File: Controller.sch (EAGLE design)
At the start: 40 parts, among them SW1 MULTICOLOR_BUTTON, SW2 MULTICOLOR_BUTTON, SW3 MULTICOLOR_BUTTON, SW4 MULTICOLOR_BUTTON, SW5 MULTICOLOR_BUTTON, SW6 MULTICOLOR_BUTTON, SW7 MULTICOLOR_BUTTON, SW8 MULTICOLOR_BUTTON

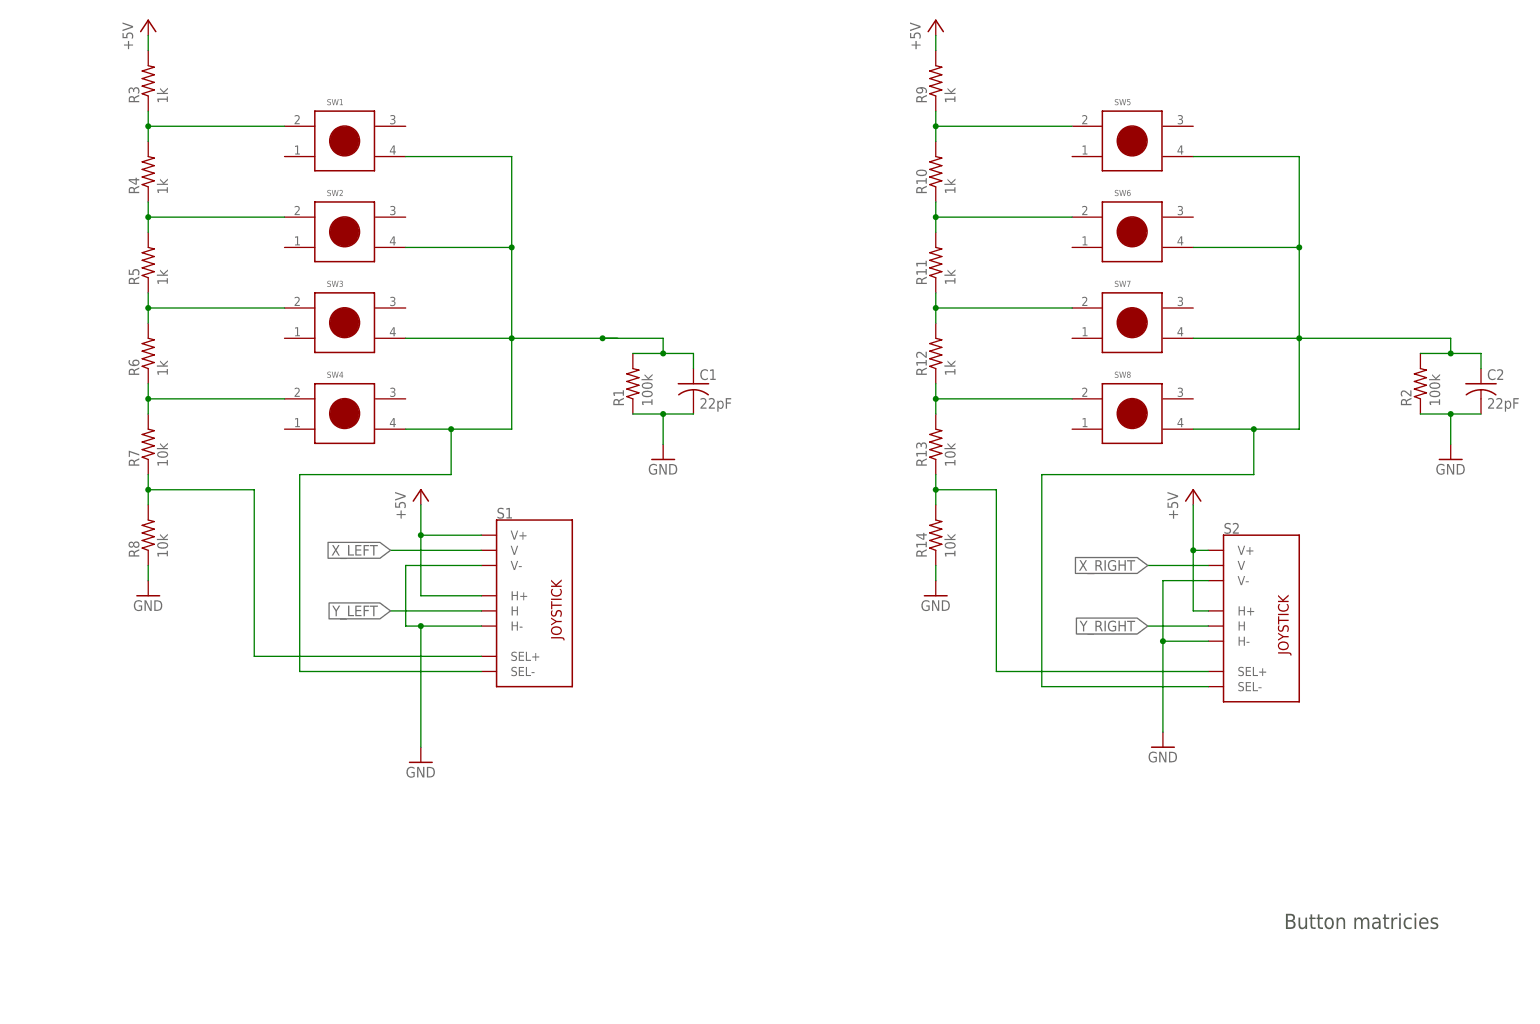
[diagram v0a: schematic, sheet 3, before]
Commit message: Redid debounce filter and added unity gain buffer. Added Xbee and logic level shifter for RX and TX
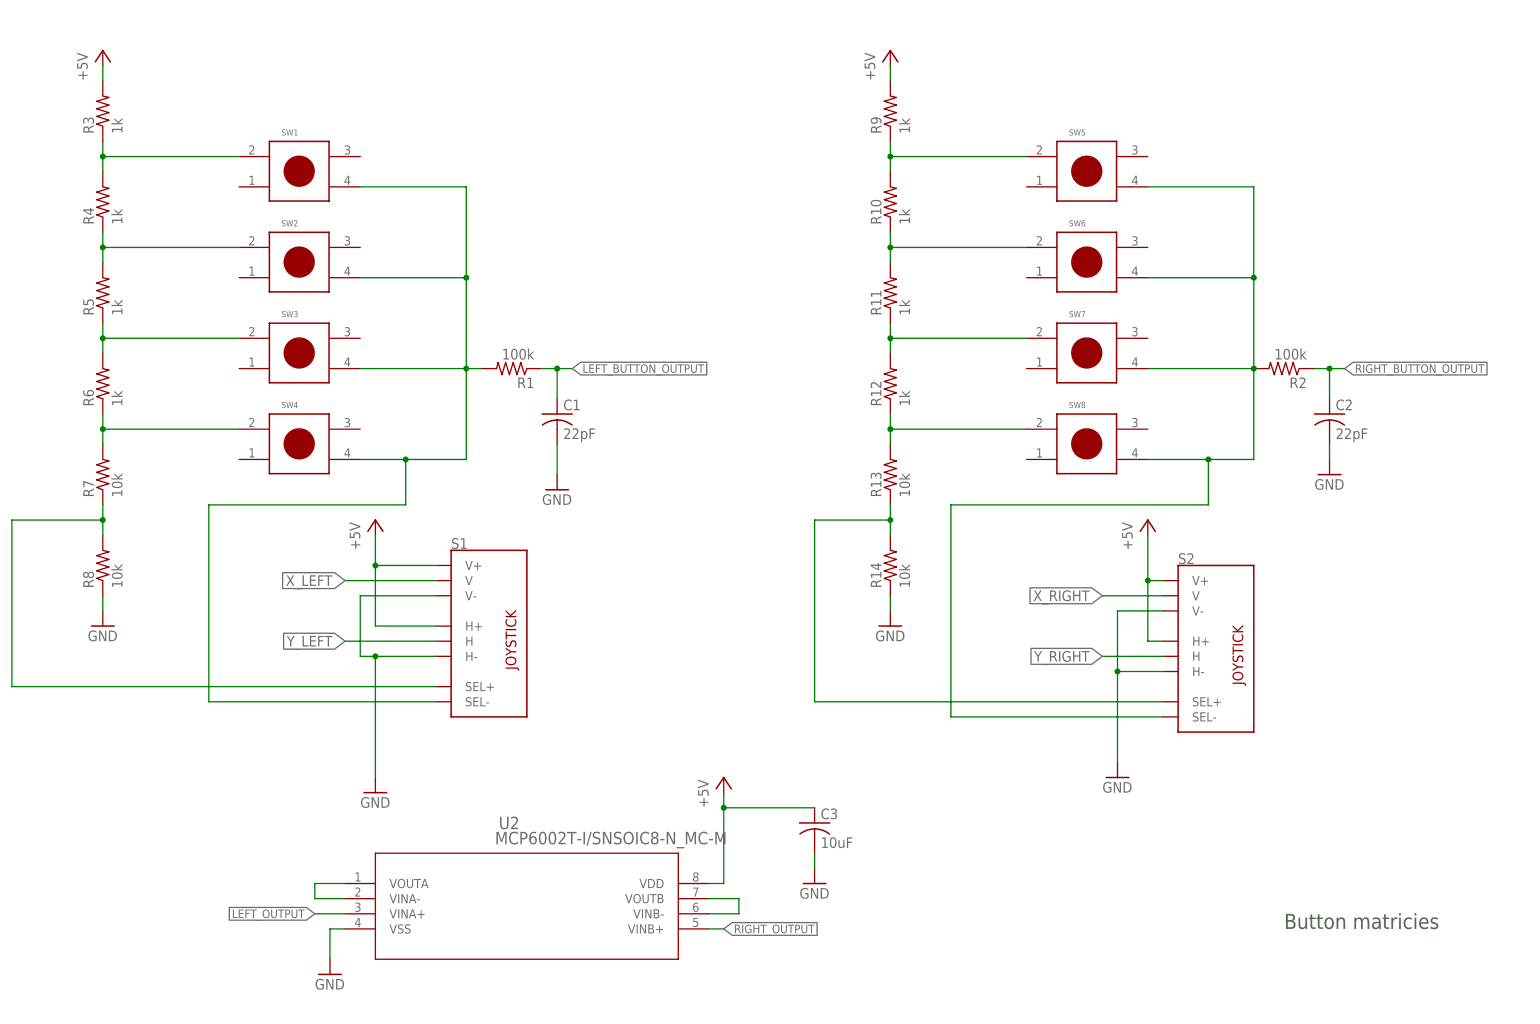
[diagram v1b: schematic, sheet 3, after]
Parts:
- removed U$1: NANO_SKELETON_FOR_PRATIK, Micah's Shit For Pratik:NANO_SKELETON_FOR_PRATIK
- added C3: 10uF, rcl:C-USC1206
- added U1: ATMEGA328-PU, Controller:ATMEGA328-PU
- added U2: MCP6002T-I/SNSOIC8-N_MC-M, Controller:MCP6002T-I/SNSOIC8-N_MC-M
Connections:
- removed net BUT_OUT_L: U$1.1/TX
- removed net BUT_OUT_R: U$1.0/RX
- removed net N$1: C1.1, R1.2, S1.SEL-, SW1.P$4, SW2.P$4, SW3.P$4, SW4.P$4
- new net LEFT_BUTTON_OUTPUT: C1.1, R1.1
- new net LEFT_OUTPUT: R1.2, S1.SEL-, SW1.P$4, SW2.P$4, SW3.P$4, SW4.P$4, U1.PB1/OC1A/PCINT1, U1.PC0/ADC0/PCINT8, U2.VINA+
- new net N$13: U2.VINB-, U2.VOUTB
- new net RIGHT_BUTTON_OUTPUT: C2.1, R2.1
- new net RIGHT_OUTPUT: R2.2, S2.SEL-, SW5.P$4, SW6.P$4, SW7.P$4, SW8.P$4, U1.PC1/ADC1/PCINT9, U1.PCINT23/AIN1/PD7, U2.VINB+
- net +5V: now also C3.1, U1.AREF, U1.VCC, U2.VDD
- net 3.3: no longer U$1.3.3V
- net 5V: no longer U$1.+5V
- net BUT_OUT_BUMP: no longer U$1.7
- net GND: now also C3.2, U1.GND, U1.GND_2, U2.VSS; no longer R1.1, R2.1, U$1.GND, U$1.GND2.0
- net N$2: now also U2.VINA-, U2.VOUTA; no longer C2.1, R2.2, S2.SEL-, SW5.P$4, SW6.P$4, SW7.P$4, SW8.P$4
- net XBEE_DIN: no longer U$1.2/SDA
- net XBEE_DOUT: no longer U$1.3(PWM)/SCL
- net X_LEFT: now also U1.PC2/ADC2/PCINT10
- net X_RIGHT: now also U1.PC4/ADC4/SDA/PCINT12
- net Y_LEFT: now also U1.PC3/ADC3/PCINT11
- net Y_RIGHT: now also U1.PC5/ADC5/SCL/PCINT13
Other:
- moved on the sheet: C1, C2, R1, R10, R11, R12, R13, R14, R2, R3, R4, R5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

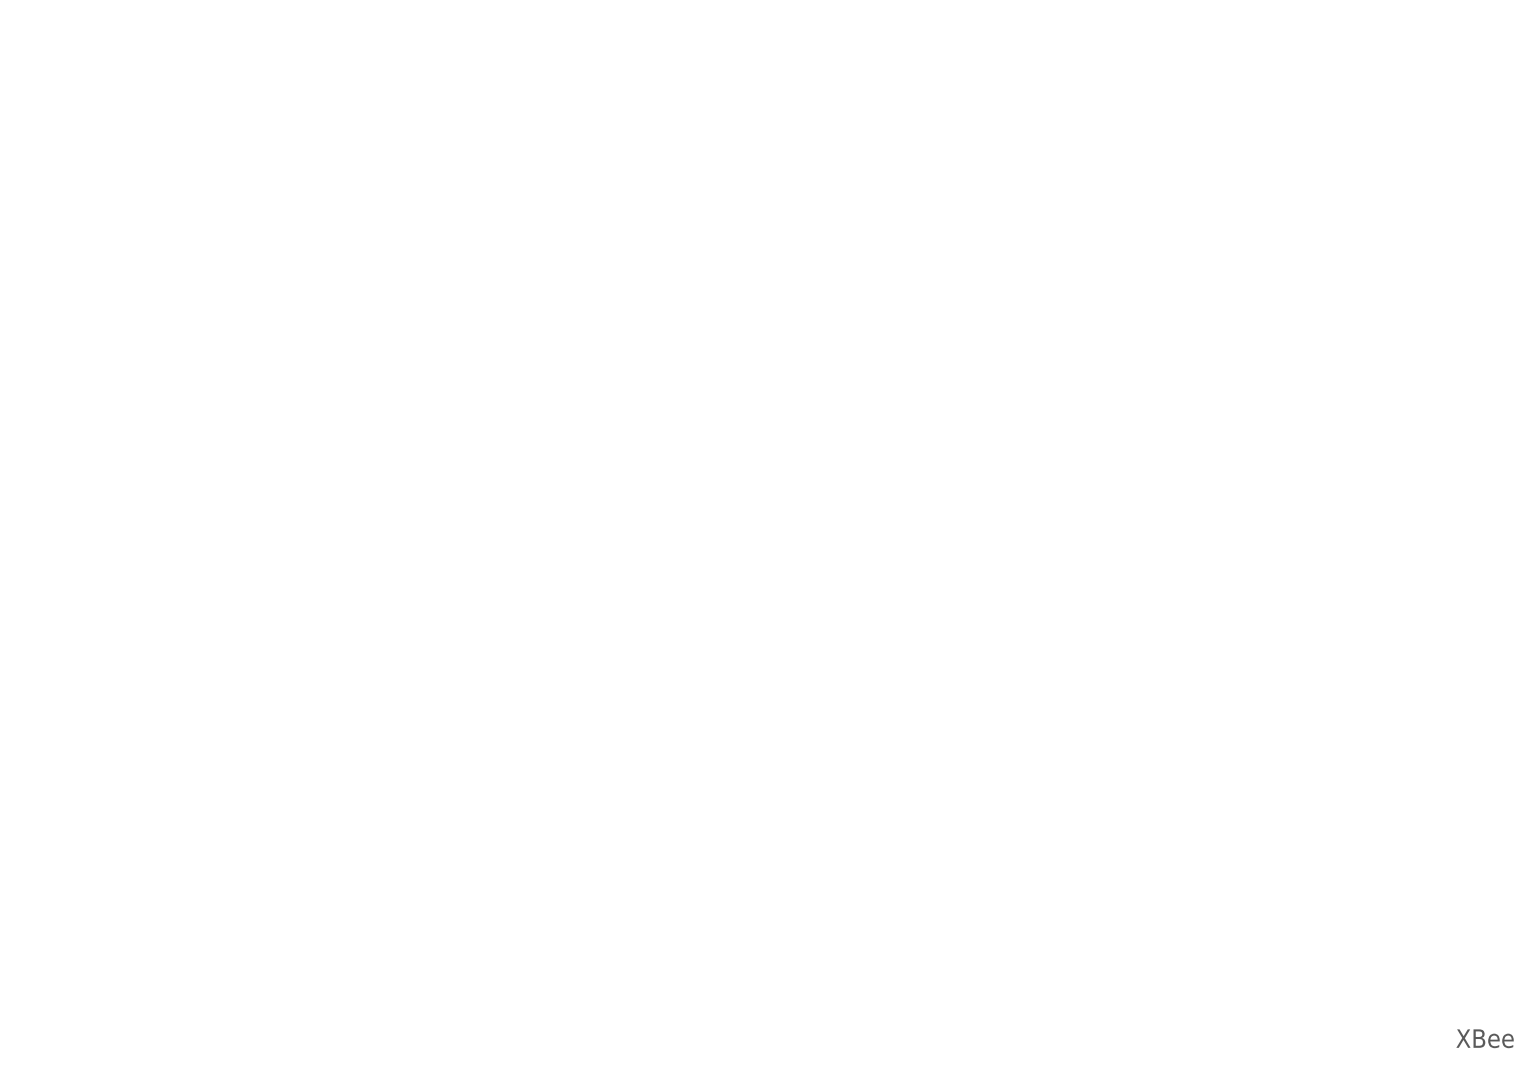
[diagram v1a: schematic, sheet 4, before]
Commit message: Fixed connection error in Low Pass filter
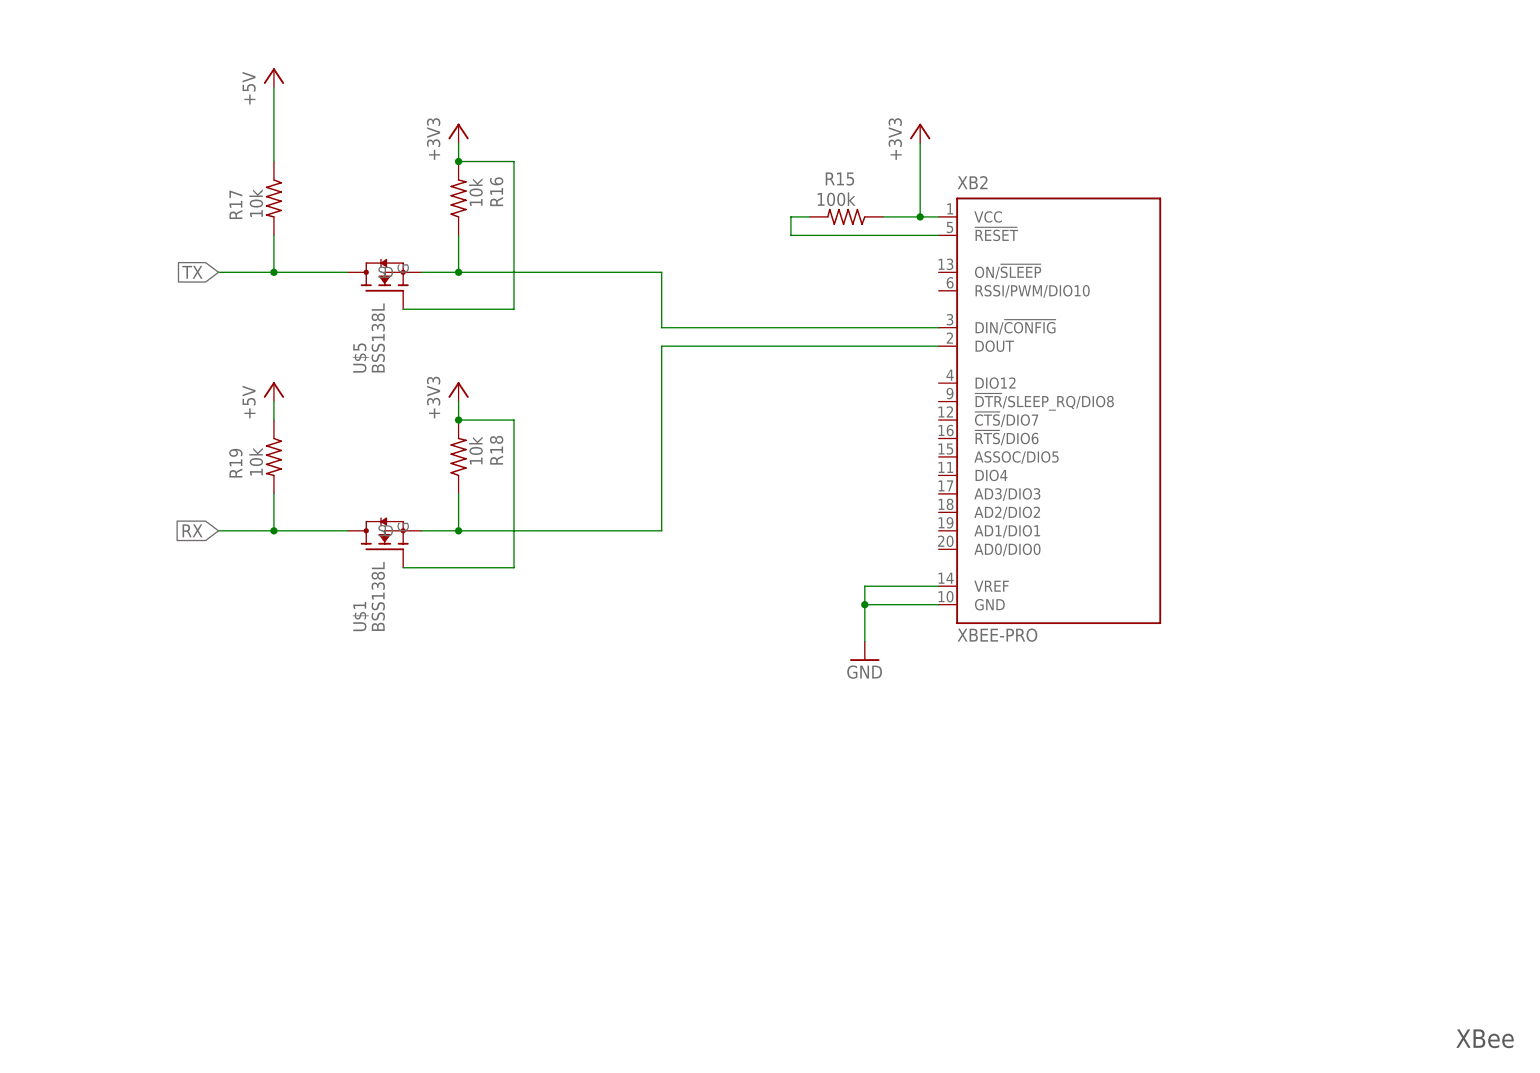
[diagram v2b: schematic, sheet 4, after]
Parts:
- removed XB1: XBEE-PRO, xbee:XBEE-PRO
- added C4, C6: 22pF, rcl:C-USC1206
- added R15: 100k, rcl:R-US_R1206
- added R16, R17, R18, R19: 10k, rcl:R-US_R1206
- added U$1, U$5: BSS138L, BSS138L:BSS138L
- added XB2: XBEE-PRO, Controller:XBEE-PRO
- added Y1: ECS-160-20-4X, ECS-160-20-4X:ECS-160-20-4X
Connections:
- removed net 3.3: XB1.!RESET, XB1.VCC
- removed net N$13: U2.VINB-, U2.VOUTB
- removed net N$2: U2.VINA-, U2.VOUTA
- removed net XBEE_DIN: XB1.DIN/!CONFIG
- removed net XBEE_DOUT: XB1.DOUT
- new net +3V3: R15.1, R16.2, R18.2, U$1.G, U$5.G, XB2.VCC
- new net N$1: R15.2, XB2.!RESET
- new net N$14: R16.1, U$5.S, XB2.DIN/!CONFIG
- new net N$15: C6.1, U1.PCINT7/XTAL2/TOSC2/PB7, Y1.2
- new net N$16: C4.1, U1.PCINT6/XTAL1/TOSC1/PB6, Y1.1
- new net N$17: R18.1, U$1.S, XB2.DOUT
- new net RX: R19.2, U$1.D, U1.PCINT16/RXD/PD0
- new net TX: R17.2, U$5.D, U1.PCINT17/TXD/PD1
- net +5V: now also R17.1, R19.1
- net GND: now also C4.2, C6.2, XB2.GND, XB2.VREF; no longer XB1.GND, XB1.VREF
- net LEFT_BUTTON_OUTPUT: now also U2.VINA+
- net LEFT_OUTPUT: now also U2.VINA-, U2.VOUTA; no longer U2.VINA+
- net RIGHT_BUTTON_OUTPUT: now also U2.VINB+
- net RIGHT_OUTPUT: now also U2.VINB-, U2.VOUTB; no longer U2.VINB+
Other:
- moved on the sheet: C3

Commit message: Added more holes, did some routing added 3D models
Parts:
- removed C5: (no value), eagle-ltspice:CC1206
- removed R31, R32, R33, R34, R35: (no value), resistor:R-US_M1206
- removed S3, S4: (no value), SparkFun-Switches:SWITCH-SPDT-PTH-11.6X4.0MM
- removed U$2, U$3: BUMPER, Bumper:BUMPER
- removed U$4: SWITCH, 3 Pole Double Throw Switch:SWITCH
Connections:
- removed net 5V: R31.2, U$2.IN
- removed net BUT_OUT_BUMP: C5.1, R35.2, S3.S, S4.S, U$2.OUT, U$3.OUT
- removed net N$19: R31.1, R32.2, U$3.IN
- removed net N$20: R32.1, R33.2, S3.P
- removed net N$21: R33.1, R34.2, S4.P
- net GND: no longer C5.2, R34.1, R35.1, U$2.GROUND, U$2.GROUND1, U$3.GROUND, U$3.GROUND1

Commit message: Changes
Added more 3D models. Changed to a ATMega2560
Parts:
- removed C4, C6: 22pF, rcl:C-USC1206
- removed U1: ATMEGA328-PU, Controller:ATMEGA328-PU
- removed Y1: ECS-160-20-4X, ECS-160-20-4X:ECS-160-20-4X
- added C5: 22pF, rcl:C-USC1206
- added R20, R21, R22, R23: 1k, rcl:R-US_R1206
- added R24, R25: 10k, rcl:R-US_R1206
- added R26: 100k, rcl:R-US_R1206
- added SW10, SW9: MY_LBR_SPSTSWITCH, Controller:MY_LBR_SPSTSWITCH
- added U$2, U$3: BUMPER_BUMPER, Controller:BUMPER_BUMPER
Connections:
- removed net N$15: C6.1, U1.PCINT7/XTAL2/TOSC2/PB7, Y1.2
- removed net N$16: C4.1, U1.PCINT6/XTAL1/TOSC1/PB6, Y1.1
- new net N$13: R21.1, R22.2, U$3.IN
- new net N$18: R22.1, R23.2, SW9.P$1
- new net N$19: R23.1, R24.2, SW10.P$1
- new net N$2: R20.1, R21.2, U$2.IN
- new net N$20: R24.1, R25.2
- new net N$21: R26.2, SW10.P$2, SW9.P$2, U$2.OUT, U$3.OUT
- net +5V: now also R20.2; no longer U1.AREF, U1.VCC
- net GND: now also C5.2, R25.1, U$2.GROUND, U$2.GROUND1, U$3.GROUND, U$3.GROUND1; no longer C4.2, C6.2, U1.GND, U1.GND_2
- net LEFT_BUTTON_OUTPUT: now also C5.1, R26.1
- net LEFT_OUTPUT: no longer U1.PB1/OC1A/PCINT1, U1.PC0/ADC0/PCINT8
- net RIGHT_OUTPUT: no longer U1.PC1/ADC1/PCINT9, U1.PCINT23/AIN1/PD7
- net RX: no longer U1.PCINT16/RXD/PD0
- net TX: no longer U1.PCINT17/TXD/PD1
- net X_LEFT: no longer U1.PC2/ADC2/PCINT10
- net X_RIGHT: no longer U1.PC4/ADC4/SDA/PCINT12
- net Y_LEFT: no longer U1.PC3/ADC3/PCINT11
- net Y_RIGHT: no longer U1.PC5/ADC5/SCL/PCINT13

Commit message: Added Charlieplexed button matrix
Will now have to turn on PORTB bits 1:3
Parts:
- removed C1, C2: 22pF, rcl:C-USC1206
- removed R1, R2: 100k, rcl:R-US_R1206
- removed R10, R11, R12, R3, R4, R5, R6, R9: 1k, rcl:R-US_R1206
- removed R13, R14, R7, R8: 10k, rcl:R-US_R1206
- removed S5: EG4208A, SamacSys_Parts:EG4208A
- added U$4, U$6: BUMPER_BUMPER, Controller:BUMPER_BUMPER
- added U1: ATMEGA328-PU, Controller:ATMEGA328-PU
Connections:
- removed net N$10: R11.1, R12.2, SW7.P$1
- removed net N$11: R12.1, R13.2, SW8.P$1
- removed net N$12: R13.1, R14.2, S2.SEL+
- removed net N$6: R4.1, R5.2, SW2.P$1
- removed net N$7: R5.1, R6.2, SW3.P$1
- removed net N$8: R6.1, R7.2, SW4.P$1
- removed net N$9: R7.1, R8.2, S1.SEL+
- new net C1: S1.SEL-, SW1.P$4, SW5.P$4
- new net C2: S2.SEL-, SW2.P$4, SW6.P$4
- new net C3: SW3.P$4, SW7.P$4, U$4.GROUND
- new net C4: SW4.P$4, SW8.P$4, U$6.GROUND
- new net N$24: U1.PC1/ADC1/PCINT9
- new net N$25: U1.PC0/ADC0/PCINT8
- net +5V: now also U1.VCC; no longer R3.2, R9.2
- net GND: now also U1.GND, U1.GND_2; no longer C1.2, C2.2, R14.1, R8.1
- net LEFT_BUTTON_OUTPUT: no longer C1.1, R1.1
- net LEFT_OUTPUT: no longer R1.2, S1.SEL-, SW1.P$4, SW2.P$4, SW3.P$4, SW4.P$4
- net N$3: now also SW1.P$1, SW2.P$1, SW3.P$1, SW4.P$1; no longer R10.2, R9.1, SW5.P$1
- net N$4: now also SW5.P$1, SW7.P$1, SW8.P$1; no longer R10.1, R11.2
- net N$5: now also S1.SEL+, S2.SEL+, U$4.IN, U$6.IN; no longer R3.1, R4.2, SW1.P$1
- net RIGHT_BUTTON_OUTPUT: no longer C2.1, R2.1
- net RIGHT_OUTPUT: no longer R2.2, S2.SEL-, SW5.P$4, SW6.P$4, SW7.P$4, SW8.P$4
- net X_LEFT: now also U1.PC5/ADC5/SCL/PCINT13
- net X_RIGHT: now also U1.PC4/ADC4/SDA/PCINT12
- net Y_LEFT: now also U1.PC3/ADC3/PCINT11
- net Y_RIGHT: now also U1.PC2/ADC2/PCINT10
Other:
- note added: "Atmega2560"
- note removed: "Atmega328p"
- note removed: "Power Connections"
